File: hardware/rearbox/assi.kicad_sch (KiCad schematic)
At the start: 20 parts, among them Q1 PMV164ENE, Q5 BUK6D210

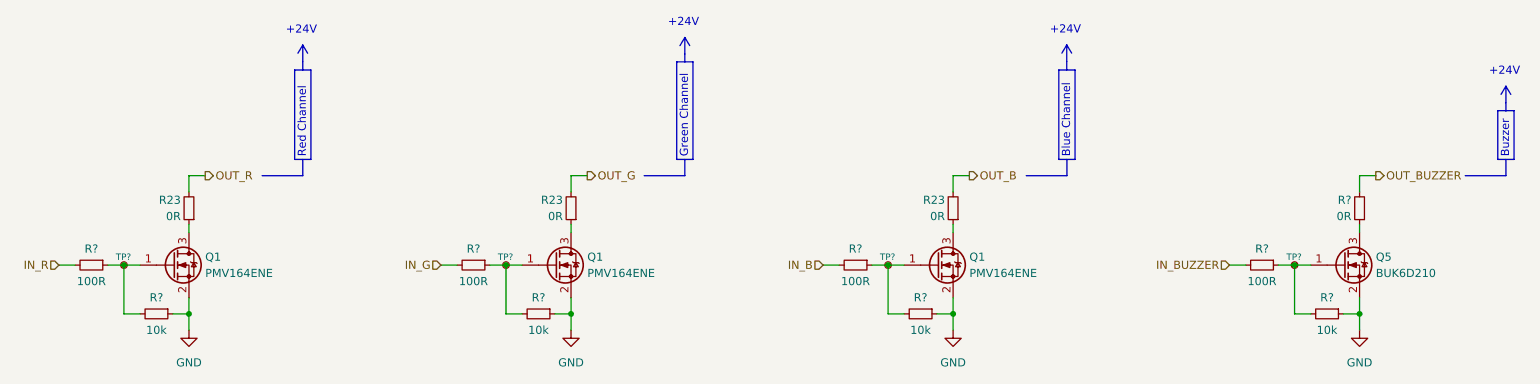
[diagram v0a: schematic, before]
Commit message: Place components on the PCB
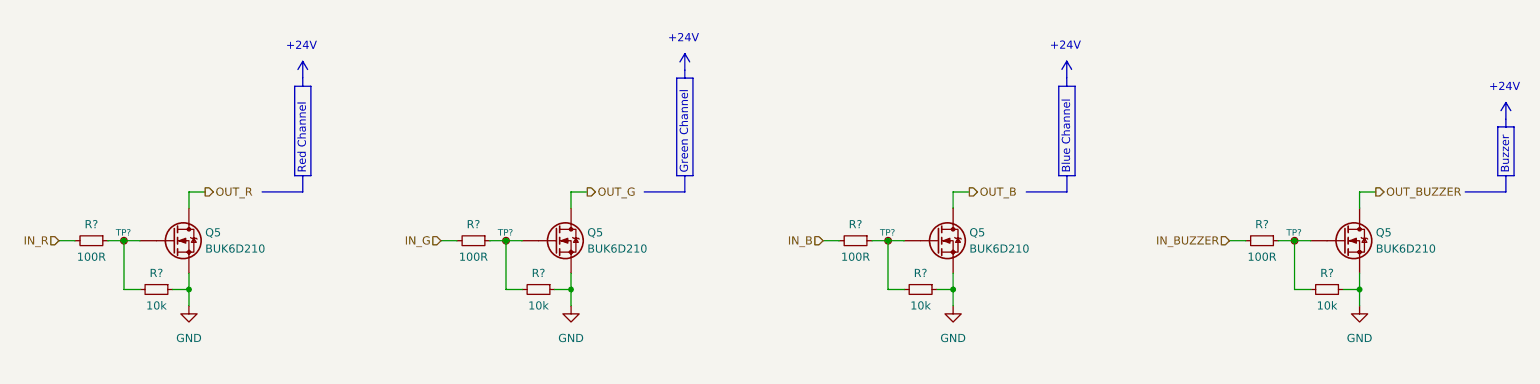
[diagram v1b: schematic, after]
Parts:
- removed Q1 (x3): PMV164ENE, Package_TO_SOT_SMD:SOT-23, symbol Device:Q_NMOS_GSD
- removed R23 (x3), R?: 0R, Resistor_SMD:R_0603_1608Metric, symbol Device:R_Small
- added Q5 (x3): BUK6D210, Package_DFN_QFN:Diodes_UDFN2020-6_Type-F, symbol BUK6D210:BUK6D210
- Q5: symbol Device:Q_NMOS_GSD -> BUK6D210:BUK6D210
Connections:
- net GND: now also Q5.4 (S), Q5.8 (S), Q5.4 (S), Q5.4 (S), Q5.4 (S), Q5.8 (S), Q5.8 (S), Q5.8 (S); no longer Q5.2 (S)
- net OUT_B: now also Q5.1 (D), Q5.2 (D), Q5.5 (D), Q5.6 (D), Q5.7 (D)
- net OUT_BUZZER: now also Q5.1 (D), Q5.2 (D), Q5.5 (D), Q5.6 (D), Q5.7 (D)
- net OUT_G: now also Q5.1 (D), Q5.2 (D), Q5.5 (D), Q5.6 (D), Q5.7 (D)
- net OUT_R: now also Q5.1 (D), Q5.2 (D), Q5.5 (D), Q5.6 (D), Q5.7 (D)
- net at R?.1, R?.2, TP?.1: now also Q5.3 (G) (x3)
- net at R?.1, R?.2, TP?.1: now also Q5.3 (G); no longer Q5.1 (G)
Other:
- moved on the sheet: R?, TP?

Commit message: Route PCB tracks
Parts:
- Q5: footprint Package_DFN_QFN:Diodes_UDFN2020-6_Type-F -> Local_Library:Diodes_UDFN2020-6_Type-F
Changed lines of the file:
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@@
       (effects (font (size 1.27 1.27)) (justify left))
     )
-    (property "Footprint" "Package_DFN_QFN:Diodes_UDFN2020-6_Type-F" (at 238.76 120.65 0)
+    (property "Footprint" "Local_Library:Diodes_UDFN2020-6_Type-F" (at 238.76 120.65 0)
       (effects (font (size 1.27 1.27)) hide)
     )
@@
       (effects (font (size 1.27 1.27)) (justify left))
     )
-    (property "Footprint" "Package_DFN_QFN:Diodes_UDFN2020-6_Type-F" (at 115.57 120.65 0)
+    (property "Footprint" "Local_Library:Diodes_UDFN2020-6_Type-F" (at 115.57 120.65 0)
       (effects (font (size 1.27 1.27)) hide)
     )
@@
       (effects (font (size 1.27 1.27)) (justify left))
     )
-    (property "Footprint" "Package_DFN_QFN:Diodes_UDFN2020-6_Type-F" (at 55.88 120.65 0)
+    (property "Footprint" "Local_Library:Diodes_UDFN2020-6_Type-F" (at 55.88 120.65 0)
       (effects (font (size 1.27 1.27)) hide)
     )
@@
       (effects (font (size 1.27 1.27)) (justify left))
     )
-    (property "Footprint" "Package_DFN_QFN:Diodes_UDFN2020-6_Type-F" (at 175.26 120.65 0)
-      (effects (font (size 1.27 1.27)) hide)
-    )
+    (property "Footprint" "Local_Library:Diodes_UDFN2020-6_Type-F" (at 175.26 120.65 0)
+      (effects (font (size 1.27 1.27)) hide)
+    )

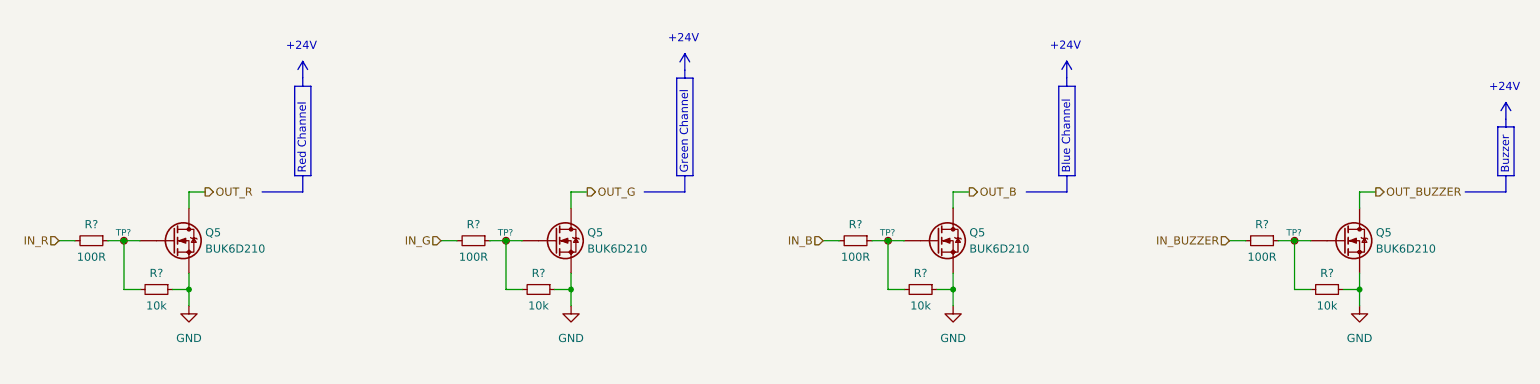
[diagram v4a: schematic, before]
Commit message: Route the tracks on the connector PCB
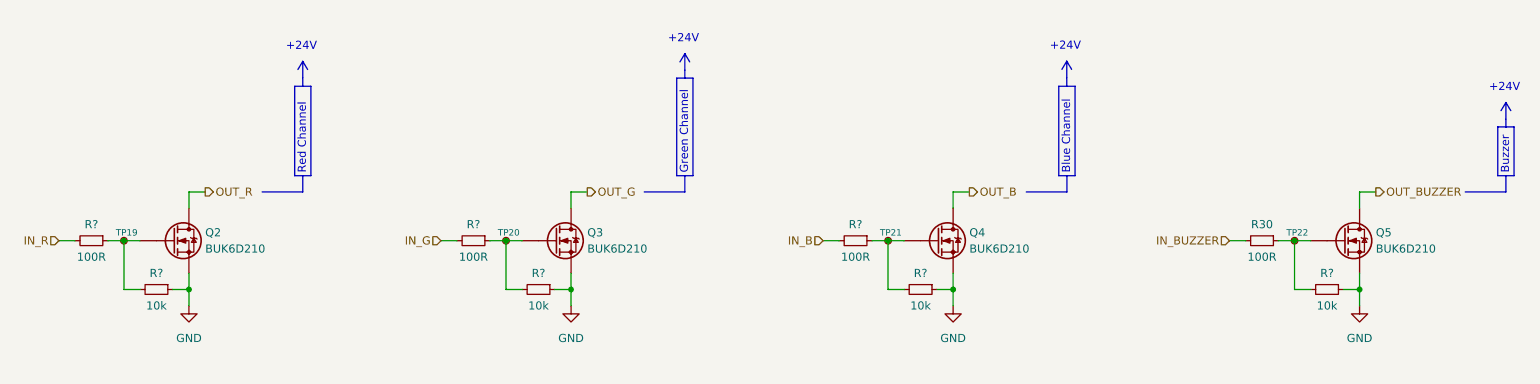
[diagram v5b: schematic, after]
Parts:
- gave numbers to parts that had none: 5
- renumbered Q5 to Q2, Q5 to Q3, Q5 to Q4

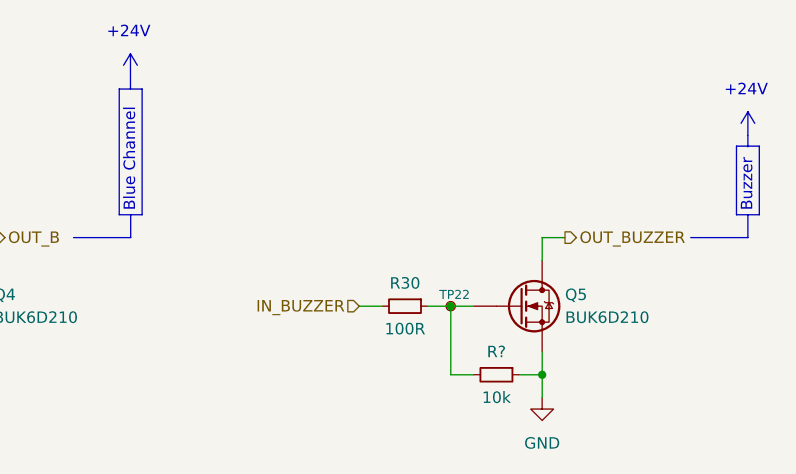
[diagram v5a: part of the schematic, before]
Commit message: Fix measurement bridges polarity
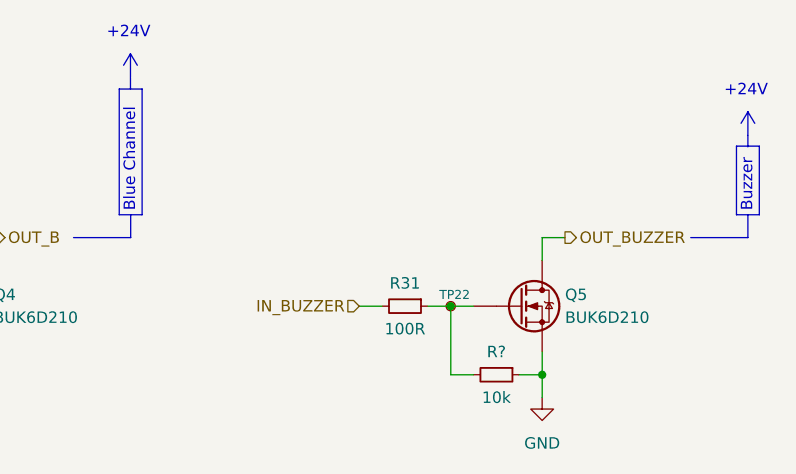
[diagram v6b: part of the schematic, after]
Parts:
- renumbered R30 to R31
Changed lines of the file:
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@@
   (title_block
     (title "Autonomous System Status Indicator")
-    (date "2023-11-17")
+    (date "2024-04-28")
     (rev "${REVISION}")
     (company "Author: I. Kajdan")
@@
       (project "rearbox"
         (path "/b652b05a-4e3d-4ad1-b032-18886abe7d45/23ffbfb4-d932-48bb-a16b-e7ed705895f1"
-          (reference "R29") (unit 1)
+          (reference "R30") (unit 1)
         )
       )
@@
       (project "rearbox"
         (path "/b652b05a-4e3d-4ad1-b032-18886abe7d45/23ffbfb4-d932-48bb-a16b-e7ed705895f1"
-          (reference "R28") (unit 1)
+          (reference "R29") (unit 1)
         )
       )
@@
       (project "rearbox"
         (path "/b652b05a-4e3d-4ad1-b032-18886abe7d45/23ffbfb4-d932-48bb-a16b-e7ed705895f1"
-          (reference "R25") (unit 1)
+          (reference "R26") (unit 1)
         )
       )
@@
       (project "rearbox"
         (path "/b652b05a-4e3d-4ad1-b032-18886abe7d45/23ffbfb4-d932-48bb-a16b-e7ed705895f1"
-          (reference "R27") (unit 1)
+          (reference "R28") (unit 1)
         )
       )
@@
   (symbol (lib_id "power:GND") (at 57.15 118.11 0) (unit 1)
     (in_bom yes) (on_board yes) (dnp no)
-    (property "Reference" "#PWR090" (at 57.15 124.46 0)
+    (property "Reference" "#PWR091" (at 57.15 124.46 0)
       (effects (font (size 1.27 1.27)) hide)
     )
@@
       (project "rearbox"
         (path "/b652b05a-4e3d-4ad1-b032-18886abe7d45/23ffbfb4-d932-48bb-a16b-e7ed705895f1"
-          (reference "#PWR090") (unit 1)
+          (reference "#PWR091") (unit 1)
         )
       )
@@
   (symbol (lib_id "Device:R_Small") (at 224.79 107.95 270) (unit 1)
     (in_bom yes) (on_board yes) (dnp no)
-    (property "Reference" "R30" (at 224.79 105.41 90)
+    (property "Reference" "R31" (at 224.79 105.41 90)
       (effects (font (size 1.27 1.27)))
     )
@@
       (project "rearbox"
         (path "/b652b05a-4e3d-4ad1-b032-18886abe7d45/23ffbfb4-d932-48bb-a16b-e7ed705895f1"
-          (reference "R30") (unit 1)
+          (reference "R31") (unit 1)
         )
       )
@@
       (project "rearbox"
         (path "/b652b05a-4e3d-4ad1-b032-18886abe7d45/23ffbfb4-d932-48bb-a16b-e7ed705895f1"
-          (reference "R24") (unit 1)
+          (reference "R25") (unit 1)
         )
       )
@@
   (symbol (lib_id "power:GND") (at 116.84 118.11 0) (unit 1)
     (in_bom yes) (on_board yes) (dnp no)
-    (property "Reference" "#PWR091" (at 116.84 124.46 0)
+    (property "Reference" "#PWR092" (at 116.84 124.46 0)
       (effects (font (size 1.27 1.27)) hide)
     )
@@
       (project "rearbox"
         (path "/b652b05a-4e3d-4ad1-b032-18886abe7d45/23ffbfb4-d932-48bb-a16b-e7ed705895f1"
-          (reference "#PWR091") (unit 1)
+          (reference "#PWR092") (unit 1)
         )
       )
@@
       (project "rearbox"
         (path "/b652b05a-4e3d-4ad1-b032-18886abe7d45/23ffbfb4-d932-48bb-a16b-e7ed705895f1"
-          (reference "R31") (unit 1)
+          (reference "R32") (unit 1)
         )
       )
@@
   (symbol (lib_id "power:GND") (at 240.03 118.11 0) (unit 1)
     (in_bom yes) (on_board yes) (dnp no)
-    (property "Reference" "#PWR093" (at 240.03 124.46 0)
+    (property "Reference" "#PWR094" (at 240.03 124.46 0)
       (effects (font (size 1.27 1.27)) hide)
     )
@@
       (project "rearbox"
         (path "/b652b05a-4e3d-4ad1-b032-18886abe7d45/23ffbfb4-d932-48bb-a16b-e7ed705895f1"
-          (reference "#PWR093") (unit 1)
+          (reference "#PWR094") (unit 1)
         )
       )
@@
   (symbol (lib_id "power:GND") (at 176.53 118.11 0) (unit 1)
     (in_bom yes) (on_board yes) (dnp no)
-    (property "Reference" "#PWR092" (at 176.53 124.46 0)
+    (property "Reference" "#PWR093" (at 176.53 124.46 0)
       (effects (font (size 1.27 1.27)) hide)
     )
@@
       (project "rearbox"
         (path "/b652b05a-4e3d-4ad1-b032-18886abe7d45/23ffbfb4-d932-48bb-a16b-e7ed705895f1"
-          (reference "#PWR092") (unit 1)
+          (reference "#PWR093") (unit 1)
         )
       )
@@
       (project "rearbox"
         (path "/b652b05a-4e3d-4ad1-b032-18886abe7d45/23ffbfb4-d932-48bb-a16b-e7ed705895f1"
-          (reference "R26") (unit 1)
-        )
-      )
+          (reference "R27") (unit 1)
+        )
+      )
